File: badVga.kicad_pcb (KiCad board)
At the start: 4 copper layers, 139.3 x 102.4 mm, 47 parts, among them J1 VGA, J10 Conn_01x04, J12 Conn_01x08, J13 Conn_01x08, J14 Conn_01x08, J15 Conn_01x08, J16 Conn_01x16, J2 Conn_01x06, J3 Conn_01x16, J4 Conn_01x08, J5 Conn_01x08, J6 Conn_01x04, J7 Conn_01x08, J8 Conn_01x06, J9 Conn_01x08, SW1 SW_DIP_x04, U1 27C010, U11 CD74HC4040, U12 74LS20, U13 74LS20, U14 74LS30, U15 74LS30, U16 74LS00, U17 CD74HC4040, U18 74LS30, U19 74LS30, U2 74HC245, U20 74LS00, U21 IDT71342, U22 GAL16V8, U3 74LS00, U8 74HC245, Y1 TFT660

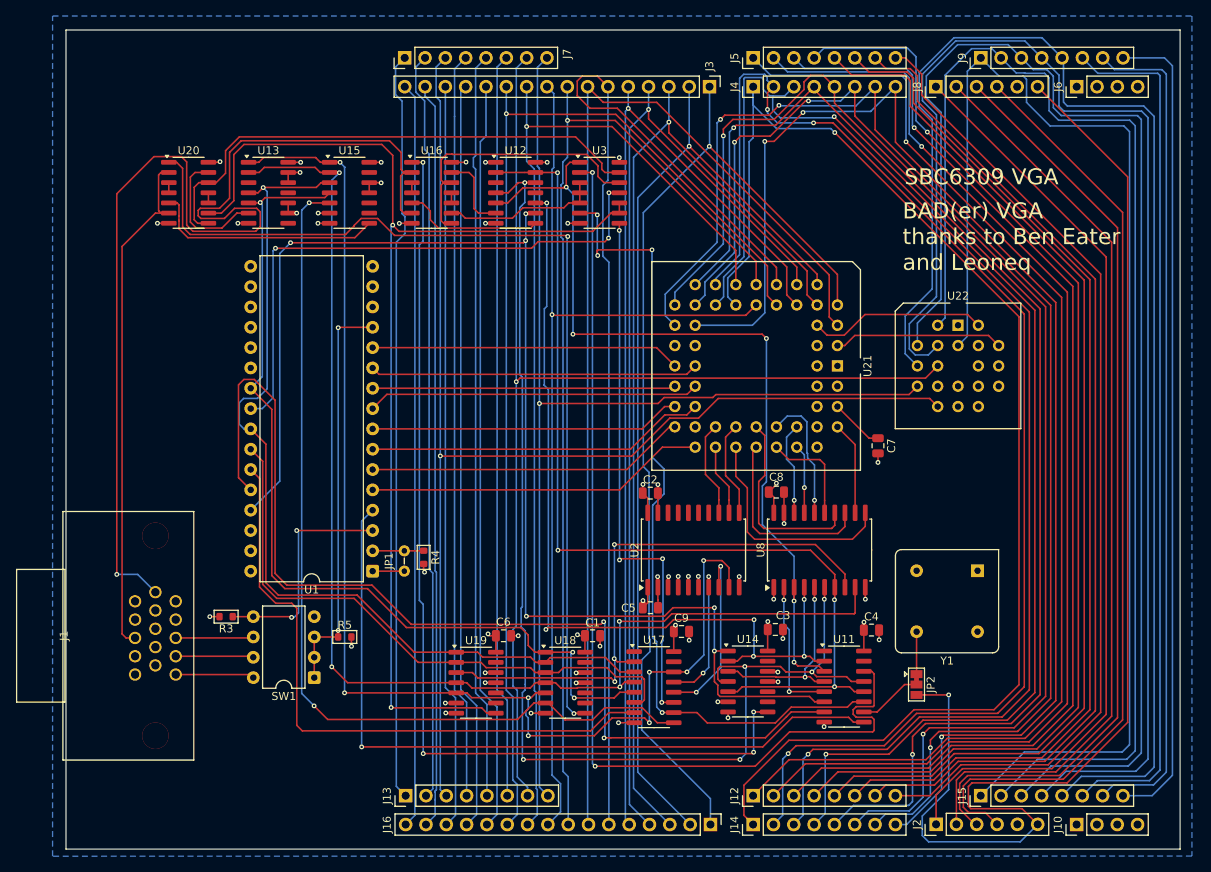
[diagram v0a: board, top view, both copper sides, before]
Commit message: fix sync signal generation
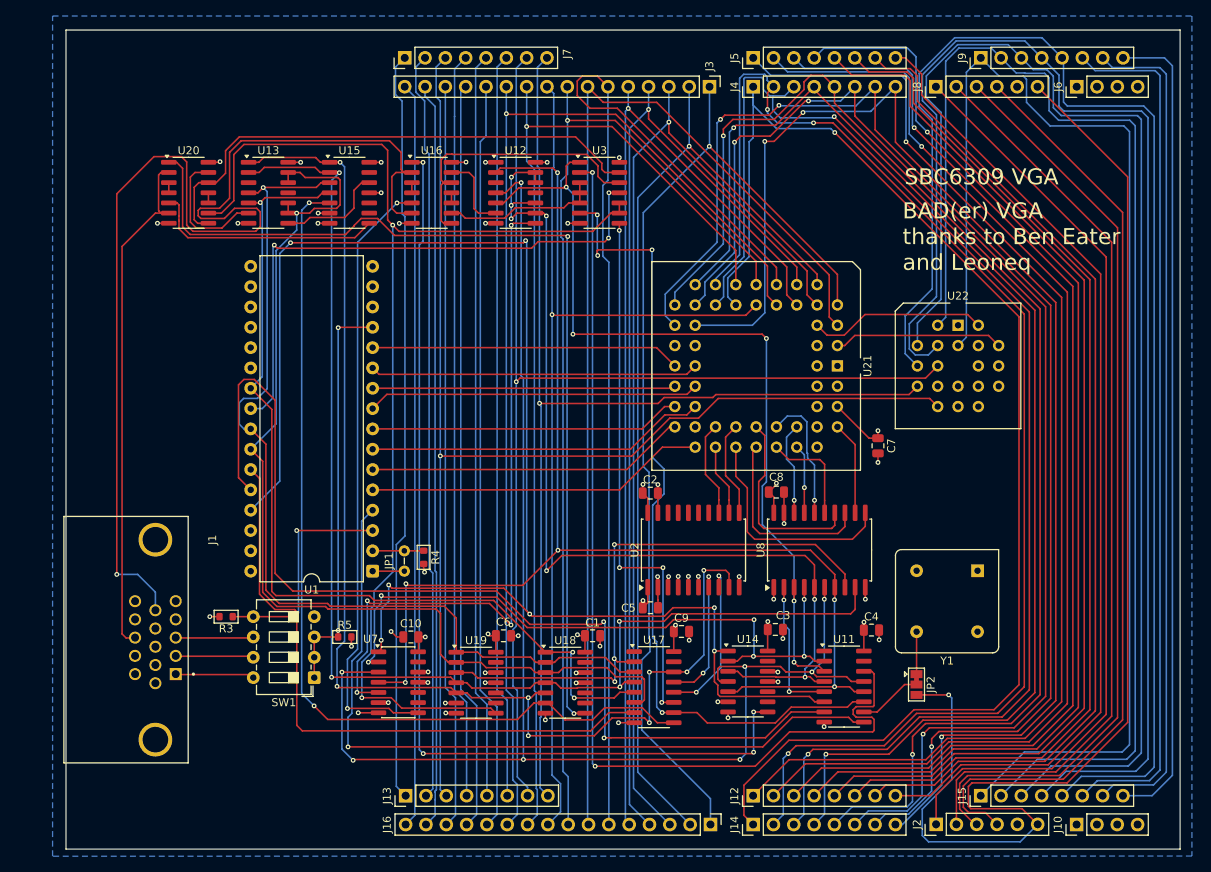
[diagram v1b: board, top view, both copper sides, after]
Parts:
- added C10: 10nF, Capacitor_SMD:C_0805_2012Metric, F.Cu at (125.9, 128.1)
- added U7: 74LS30, Package_SO:SOIC-14_3.9x8.7mm_P1.27mm, F.Cu at (124.3, 133.8)
- J1: footprint Library:CONN_AHDF15A-KG-TAXB_ASM -> Library:AMPHENOL_ICD15S13E4GX00LF
- SW1: footprint Package_DIP:DIP-8_W7.62mm -> Button_Switch_THT:SW_DIP_SPSTx04_Slide_6.7x11.72mm_W7.62mm_P2.54mm_LowProfile
- moved J1 11.4 mm to (94.0, 128.5), turned to -90 degrees
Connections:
- U12 pad 10: HB2 -> HB3
- U12 pad 12: HB4 -> HB3
- U12 pad 13: HB5 -> HB3
- U12 pad 9: HB12 -> HB3
- U13 pad 10: GND -> VB2
- U13 pad 12: GND -> VB2
- U13 pad 13: GND -> VB2
- U13 pad 8: unconnected-(U13-Pad8) -> Net-(U13-Pad8)
- U13 pad 9: GND -> VB2
- U15 pad 12: +5V -> Net-(U13-Pad8)
- U16 pad 5: Net-(U12-Pad8) -> Net-(U16-Pad5)
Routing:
- net HB3: track 24.3 -> 123.6 mm, vias 2 -> 7
- net Net-(U16-Pad5): track 0.00 -> 76.7 mm, vias 0 -> 2
- net Net-(U12-Pad8): track 17.6 -> 87.1 mm, vias 0 -> 4
- net VB2: track 74.6 -> 129.6 mm, vias 0 -> 1
- net HB5: track 122.3 -> 159.4 mm, vias 4 -> 6
- net HB4: track 150.6 -> 185.6 mm, vias 6 -> 8
- net HB12: track 166.9 -> 190.0 mm, vias 6 -> 7
- net HB2: track 107.5 -> 84.7 mm
- net Net-(U13-Pad8): track 0.00 -> 13.5 mm
- net +5V: track 65.2 -> 71.3 mm, vias 26 -> 31
- net Net-(U19-Pad8): track 143.9 -> 148.4 mm
- net HSYNC: track 136.0 -> 140.3 mm
- net VB4: track 115.7 -> 118.8 mm
- net HB10: track 94.7 -> 97.1 mm
- net VB8: track 22.5 -> 20.2 mm
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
